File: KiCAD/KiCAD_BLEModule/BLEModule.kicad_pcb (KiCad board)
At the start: 2 copper layers, 19.4 x 33.6 mm, 20 parts, among them J1 CastellatedPinHeader1.27mm_12, J2 CastellatedPinHeader1.27mm_12, J3 CastellatedPinHeader1.27mm_12, U1 nRF52832-QFAA, Y1 Y_32MHz

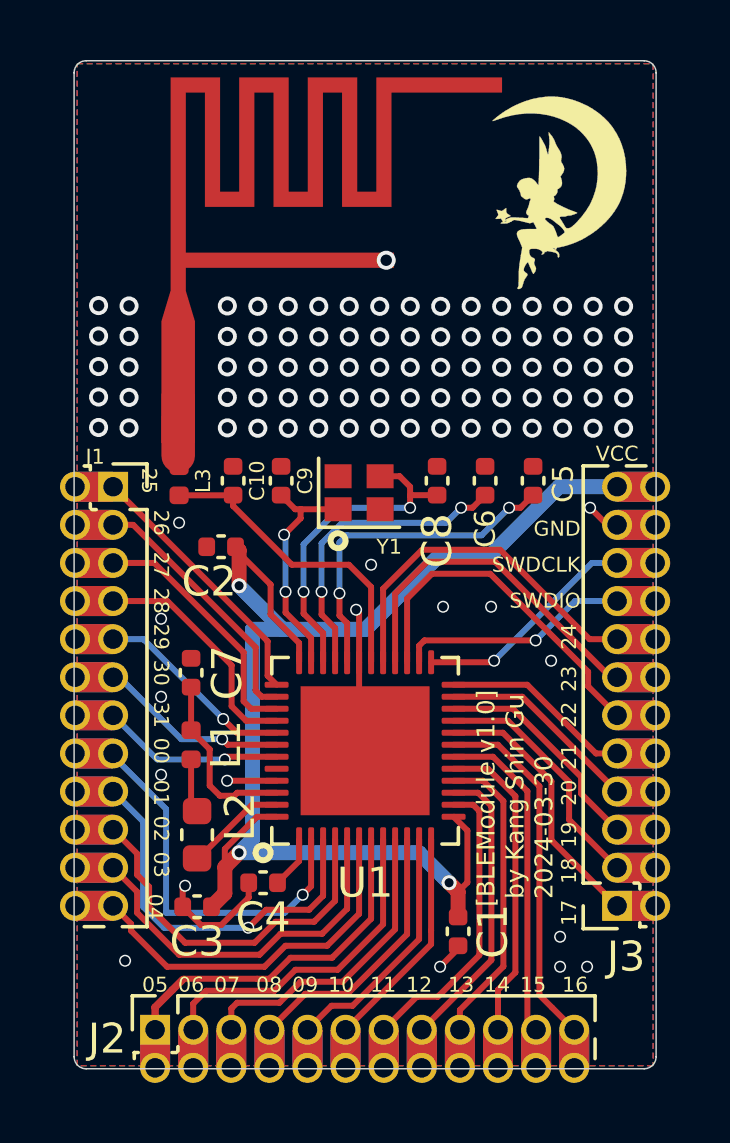
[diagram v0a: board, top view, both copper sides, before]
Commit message: KSG : 아트워크 프린트 오기 수정
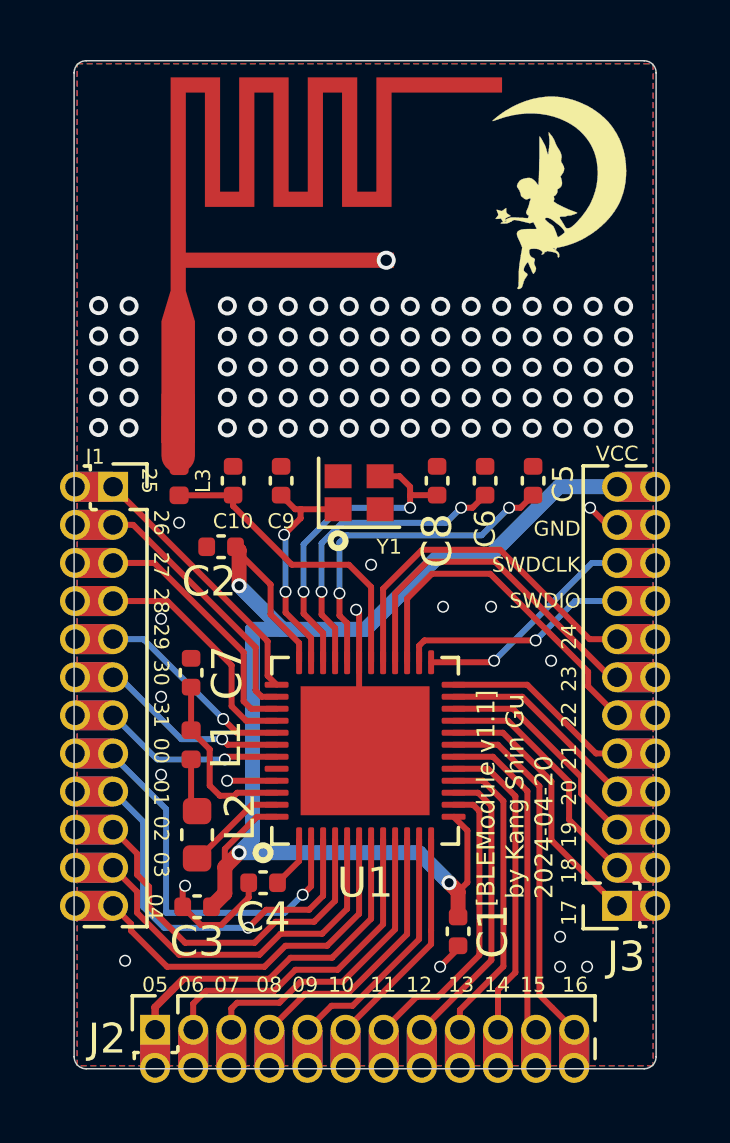
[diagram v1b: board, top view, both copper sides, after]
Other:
- board text added: "[BLEModule v1.1] by Kang Shin Gu 2024-04-20"
- board text removed: "[BLEModule v1.0] by Kang Shin Gu 2024-03-30"
